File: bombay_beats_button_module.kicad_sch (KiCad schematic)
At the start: 2 parts

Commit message: one sided version
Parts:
- btn_1: Part number (none) -> C2844397; part_number C2844397 -> (none)
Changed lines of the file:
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@@
 			)
 		)
-		(property "part_number" "C2844397"
+		(property "Part number" "C2844397"
+			(at 54.61 45.72 0)
+			(effects
+				(font
+					(size 1.27 1.27)
+				)
+				(hide yes)
+			)
+		)
+		(property "part_number" ""
 			(at 54.61 45.72 0)
 			(effects
@@
 			(effects
 				(font
+					(size 1.27 1.27)
+				)
+				(hide yes)
+			)
+		)
+		(property "part_number" ""
+			(at 72.39 43.18 0)
+			(effects
+				(font

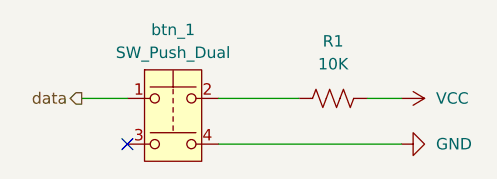
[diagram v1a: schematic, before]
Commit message: finalize one sided smd version
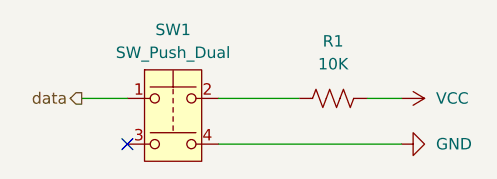
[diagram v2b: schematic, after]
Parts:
- R1: LCSC Part #  (none) -> C328335; Part number C328335 -> (none)
- SW1: renamed from btn_1; LCSC Part #  (none) -> C2844397; Part number C2844397 -> (none)
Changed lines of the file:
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@@
 		(dnp no)
 		(fields_autoplaced yes)
-		(property "Reference" "btn_1"
+		(property "Reference" "SW1"
 			(at 54.61 35.56 0)
 			(effects
@@
 			)
 		)
-		(property "Part number" "C2844397"
-			(at 54.61 45.72 0)
-			(effects
-				(font
-					(size 1.27 1.27)
-				)
-				(hide yes)
-			)
-		)
-		(property "part_number" ""
+		(property "LCSC Part # " "C2844397"
 			(at 54.61 45.72 0)
 			(effects
@@
 			(project "bombay_beats"
 				(path "/4c45dfb4-652a-4480-93b8-479ee7e6e64f/41fe3c3c-d1ff-4dee-bcd6-a6a4353b17df"
-					(reference "btn_1")
+					(reference "SW1")
 					(unit 1)
 				)
 				(path "/4c45dfb4-652a-4480-93b8-479ee7e6e64f/7aaabf71-2530-4c47-af9b-1b3a3fcc0dbe"
-					(reference "btn_2")
+					(reference "SW2")
 					(unit 1)
 				)
 				(path "/4c45dfb4-652a-4480-93b8-479ee7e6e64f/ec4cdd2b-0e1e-4a05-b262-de2f505c044c"
-					(reference "btn_3")
+					(reference "SW3")
 					(unit 1)
 				)
 				(path "/4c45dfb4-652a-4480-93b8-479ee7e6e64f/e3593ce6-8835-41bf-ab30-d5ac70060c5c"
-					(reference "btn_4")
+					(reference "SW4")
 					(unit 1)
 				)
 				(path "/4c45dfb4-652a-4480-93b8-479ee7e6e64f/114b802e-8df2-4f86-81c6-f2910a089ccb"
-					(reference "btn_5")
+					(reference "SW5")
 					(unit 1)
 				)
 				(path "/4c45dfb4-652a-4480-93b8-479ee7e6e64f/3f1c5d04-286c-4548-a304-525f1e16d060"
-					(reference "btn_6")
+					(reference "SW6")
 					(unit 1)
 				)
 				(path "/4c45dfb4-652a-4480-93b8-479ee7e6e64f/a52ff669-c3bc-4390-b97a-b0f65946cfe0"
-					(reference "btn_7")
+					(reference "SW7")
 					(unit 1)
 				)
 				(path "/4c45dfb4-652a-4480-93b8-479ee7e6e64f/fb229351-4db1-41bb-ad69-0d469bb47317"
-					(reference "btn_8")
+					(reference "SW8")
 					(unit 1)
 				)
@@
 			)
 		)
-		(property "Part number" "C328335"
+		(property "LCSC Part # " "C328335"
 			(at 72.39 43.18 90)
 			(effects
 				(font
-					(size 1.27 1.27)
-				)
-				(hide yes)
-			)
-		)
-		(property "part_number" ""
-			(at 72.39 43.18 0)
-			(effects
-				(font

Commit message: replace footprints for through hole version
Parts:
- R1: footprint Resistor_SMD:R_0201_0603Metric -> Resistor_THT:R_Axial_DIN0207_L6.3mm_D2.5mm_P10.16mm_Horizontal
- SW1: footprint CustomFootprints:4.5 Push Button Switch JLCPCB -> Button_Switch_THT:SW_PUSH_6mm_H4.3mm
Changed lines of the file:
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@@
 			)
 		)
-		(property "Footprint" "CustomFootprints:4.5 Push Button Switch JLCPCB"
+		(property "Footprint" "Button_Switch_THT:SW_PUSH_6mm_H4.3mm"
 			(at 54.61 38.1 0)
 			(effects
@@
 			)
 		)
-		(property "Footprint" "Resistor_SMD:R_0201_0603Metric"
+		(property "Footprint" "Resistor_THT:R_Axial_DIN0207_L6.3mm_D2.5mm_P10.16mm_Horizontal"
 			(at 72.644 42.164 90)
 			(effects

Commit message: production files
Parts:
- SW1: footprint Button_Switch_THT:SW_PUSH_6mm_H4.3mm -> Button_Switch_THT:SW_PUSH_6mm_4Pin
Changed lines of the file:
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@@
 			)
 		)
-		(property "Footprint" "Button_Switch_THT:SW_PUSH_6mm_H4.3mm"
+		(property "Footprint" "Button_Switch_THT:SW_PUSH_6mm_4Pin"
 			(at 54.61 38.1 0)
 			(effects
